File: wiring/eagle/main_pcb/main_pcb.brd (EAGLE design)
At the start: 100.1 x 79.8 mm, 19 parts

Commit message: Increase insulation around spacer holes to 5mm
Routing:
- net UC_TRIG: track 57.3 -> 55.6 mm
- net UC_ECHO: track 37.6 -> 36.3 mm
- net +5V: track 207.3 -> 206.0 mm
- net LED_G: track 60.9 -> 60.1 mm
- net LED_R: track 54.2 -> 53.6 mm
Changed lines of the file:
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@@
 <?xml version="1.0" encoding="utf-8"?>
 <!DOCTYPE eagle SYSTEM "eagle.dtd">
-<eagle version="9.3.0">
+<eagle version="9.3.1">
 <drawing>
 <settings>
@@
 <contactref element="PIHD" pad="2"/>
 <contactref element="POWER" pad="1"/>
-<wire x1="64.262" y1="75.946" x2="64.260965625" y2="76" width="1.5" layer="16"/>
-<wire x1="53.81" y1="76" x2="64.260965625" y2="76" width="1.5" layer="16"/>
-<wire x1="64.262" y1="75.946" x2="89.662" y2="75.946" width="1.5" layer="16"/>
+<wire x1="61.976" y1="75.946" x2="61.974965625" y2="76" width="1.5" layer="16"/>
+<wire x1="53.81" y1="76" x2="61.974965625" y2="76" width="1.5" layer="16"/>
+<wire x1="61.976" y1="75.946" x2="89.662" y2="75.946" width="1.5" layer="16"/>
 <wire x1="96.774" y1="62.3379125" x2="95.29955625" y2="60.095" width="1.5" layer="16"/>
-<via x="64.008" y="62.484" extent="1-16" drill="0.8" diameter="2"/>
-<wire x1="64.262" y1="75.946" x2="64.008" y2="75.692" width="1.5" layer="1"/>
-<wire x1="64.008" y1="75.692" x2="64.008" y2="62.484" width="1.5" layer="1"/>
-<via x="64.262" y="75.946" extent="1-16" drill="0.8" diameter="2"/>
-<wire x1="58.166" y1="62.484" x2="64.008" y2="62.484" width="1.5" layer="16"/>
+<via x="61.976" y="62.484" extent="1-16" drill="0.8" diameter="2"/>
+<wire x1="61.976" y1="75.946" x2="61.976" y2="62.484" width="1.5" layer="1"/>
+<via x="61.976" y="75.946" extent="1-16" drill="0.8" diameter="2"/>
+<wire x1="58.166" y1="62.484" x2="61.976" y2="62.484" width="1.5" layer="16"/>
 <wire x1="37.592" y1="30.988" x2="37.592" y2="40.132" width="1.5" layer="16"/>
 <wire x1="37.592" y1="40.132" x2="37.592" y2="47.244" width="1.5" layer="16"/>
@@
 <wire x1="18.181175" y1="59.69" x2="18.35840625" y2="59.51276875" width="1.5" layer="16"/>
 <wire x1="18.35840625" y1="59.51276875" x2="21.23876875" y2="59.51276875" width="1.5" layer="16"/>
-<wire x1="68.07" y1="55.13" x2="68.07" y2="58.422" width="1.5" layer="16"/>
-<wire x1="68.07" y1="58.422" x2="64.008" y2="62.484" width="1.5" layer="16"/>
+<wire x1="68.07" y1="55.13" x2="68.07" y2="56.39" width="1.5" layer="16"/>
+<wire x1="68.07" y1="56.39" x2="61.976" y2="62.484" width="1.5" layer="16"/>
 <wire x1="33.5075375" y1="47.244" x2="37.592" y2="47.244" width="1.5" layer="16"/>
 <wire x1="21.23876875" y1="59.51276875" x2="33.5075375" y2="47.244" width="1.5" layer="16"/>
@@
 <contactref element="R3" pad="1"/>
 <contactref element="PIHD" pad="12"/>
-<wire x1="70.612" y1="42.67575625" x2="70.612" y2="60.198" width="1.5" layer="16"/>
+<wire x1="70.612" y1="42.67575625" x2="70.612" y2="57.912" width="1.5" layer="16"/>
 <wire x1="58.928" y1="69.088" x2="58.928" y2="65.532" width="1.5" layer="16"/>
-<wire x1="58.928" y1="65.532" x2="65.278" y2="65.532" width="1.5" layer="16"/>
-<wire x1="65.278" y1="65.532" x2="70.612" y2="60.198" width="1.5" layer="16"/>
+<wire x1="58.928" y1="65.532" x2="62.992" y2="65.532" width="1.5" layer="16"/>
+<wire x1="62.992" y1="65.532" x2="70.612" y2="57.912" width="1.5" layer="16"/>
 <wire x1="68.07" y1="42.43" x2="70.36624375" y2="42.43" width="1.5" layer="16"/>
 <wire x1="70.36624375" y1="42.43" x2="70.612" y2="42.67575625" width="1.5" layer="16"/>
@@
 <contactref element="G_LED" pad="A"/>
 <via x="28.956" y="20.32" extent="1-16" drill="0.8" diameter="2"/>
-<via x="21.336" y="5.588" extent="1-16" drill="0.8" diameter="2"/>
-<wire x1="21.336" y1="5.588" x2="15.24" y2="5.588" width="1.5" layer="16"/>
+<via x="20.066" y="5.588" extent="1-16" drill="0.8" diameter="2"/>
+<wire x1="20.066" y1="5.588" x2="15.24" y2="5.588" width="1.5" layer="16"/>
 <wire x1="28.956" y1="20.32" x2="47.9678375" y2="20.32" width="1.5" layer="16"/>
 <wire x1="47.9678375" y1="20.32" x2="48.6898375" y2="19.598" width="1.5" layer="16"/>
 <wire x1="48.6898375" y1="19.598" x2="65.502" y2="19.598" width="1.5" layer="16"/>
 <wire x1="65.502" y1="19.598" x2="65.53" y2="19.57" width="1.5" layer="16"/>
-<wire x1="28.956" y1="14.478" x2="28.956" y2="20.32" width="1.5" layer="1"/>
-<wire x1="21.336" y1="5.588" x2="21.336" y2="6.858" width="1.5" layer="1"/>
-<wire x1="21.336" y1="6.858" x2="28.956" y2="14.478" width="1.5" layer="1"/>
+<wire x1="28.956" y1="16.51" x2="28.956" y2="20.32" width="1.5" layer="1"/>
+<wire x1="20.066" y1="5.588" x2="20.066" y2="7.62" width="1.5" layer="1"/>
+<wire x1="20.066" y1="7.62" x2="28.956" y2="16.51" width="1.5" layer="1"/>
 </signal>
 <signal name="N$11">
@@
 <contactref element="PIHD" pad="16"/>
 <wire x1="51.27" y1="76" x2="51.308" y2="72.644" width="1.5" layer="16"/>
-<wire x1="73.152" y1="40.894" x2="73.152" y2="61.976" width="1.5" layer="16"/>
-<wire x1="51.308" y1="72.644" x2="62.484" y2="72.644" width="1.5" layer="16"/>
-<wire x1="62.484" y1="72.644" x2="73.152" y2="61.976" width="1.5" layer="16"/>
+<wire x1="73.152" y1="40.894" x2="73.152" y2="59.182" width="1.5" layer="16"/>
+<wire x1="51.308" y1="72.644" x2="59.69" y2="72.644" width="1.5" layer="16"/>
+<wire x1="59.69" y1="72.644" x2="73.152" y2="59.182" width="1.5" layer="16"/>
 <wire x1="69.592" y1="37.334" x2="69.58499375" y2="37.35" width="1.5" layer="16"/>
 <wire x1="68.07" y1="37.35" x2="69.58499375" y2="37.35" width="1.5" layer="16"/>
@@
 <contactref element="R7" pad="1"/>
 <contactref element="PIHD" pad="31"/>
-<wire x1="21.082" y1="2.794" x2="24.13" y2="2.794" width="1.5" layer="16"/>
-<via x="24.13" y="2.794" extent="1-16" drill="0.8" diameter="2"/>
-<wire x1="24.13" y1="2.794" x2="24.13" y2="6.096" width="1.5" layer="1"/>
+<wire x1="21.082" y1="2.794" x2="23.114" y2="2.794" width="1.5" layer="16"/>
+<via x="23.114" y="2.794" extent="1-16" drill="0.8" diameter="2"/>
+<wire x1="23.114" y1="2.794" x2="23.114" y2="6.858" width="1.5" layer="1"/>
 <via x="31.75" y="17.018" extent="1-16" drill="0.8" diameter="2"/>
-<wire x1="24.13" y1="6.096" x2="31.75" y2="13.716" width="1.5" layer="1"/>
-<wire x1="31.75" y1="13.716" x2="31.75" y2="17.018" width="1.5" layer="1"/>
+<wire x1="23.114" y1="6.858" x2="31.75" y2="15.494" width="1.5" layer="1"/>
+<wire x1="31.75" y1="15.494" x2="31.75" y2="17.018" width="1.5" layer="1"/>
 <wire x1="31.75" y1="17.018" x2="65.518" y2="17.018" width="1.5" layer="16"/>
 <wire x1="65.518" y1="17.018" x2="65.53" y2="17.03" width="1.5" layer="16"/>
 </signal>
 <signal name="SPACER_RPI_BR">
-<via x="76.5" y="4" extent="1-16" drill="1" diameter="3"/>
+<via x="76.5" y="4" extent="1-16" drill="1" diameter="5"/>
 </signal>
 <signal name="SPACER_PCB_L">
-<via x="12.5" y="71.5" extent="1-16" drill="1" diameter="4"/>
+<via x="12.5" y="71.5" extent="1-16" drill="1" diameter="5"/>
 </signal>
 <signal name="SPACER_PCB_R">
-<via x="87.5" y="71.5" extent="1-16" drill="1" diameter="4"/>
+<via x="87.5" y="71.5" extent="1-16" drill="1" diameter="5"/>
 </signal>
 <signal name="SPACER_RPI_FL">
-<via x="27.5" y="62" extent="1-16" drill="1" diameter="3"/>
+<via x="27.5" y="62" extent="1-16" drill="1" diameter="5"/>
 </signal>
 <signal name="SPACER_RPI_FR">
-<via x="76.5" y="62" extent="1-16" drill="1" diameter="3"/>
+<via x="76.5" y="62" extent="1-16" drill="1" diameter="5"/>
 </signal>
 <signal name="SPACER_RPI_BL">
-<via x="27.5" y="4" extent="1-16" drill="1" diameter="3"/>
+<via x="27.5" y="4" extent="1-16" drill="1" diameter="5"/>
 </signal>
 </signals>

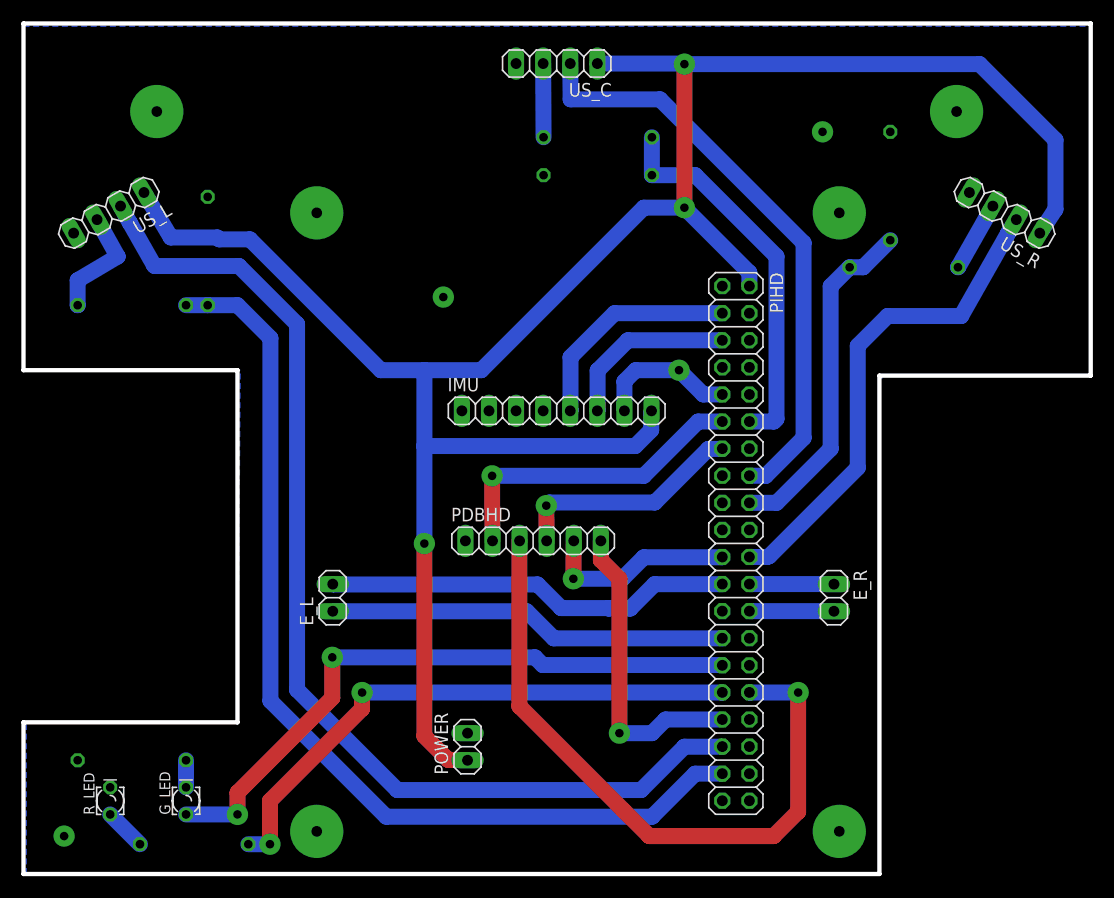
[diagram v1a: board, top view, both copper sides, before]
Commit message: Add IMU spacer and other minor adjustments
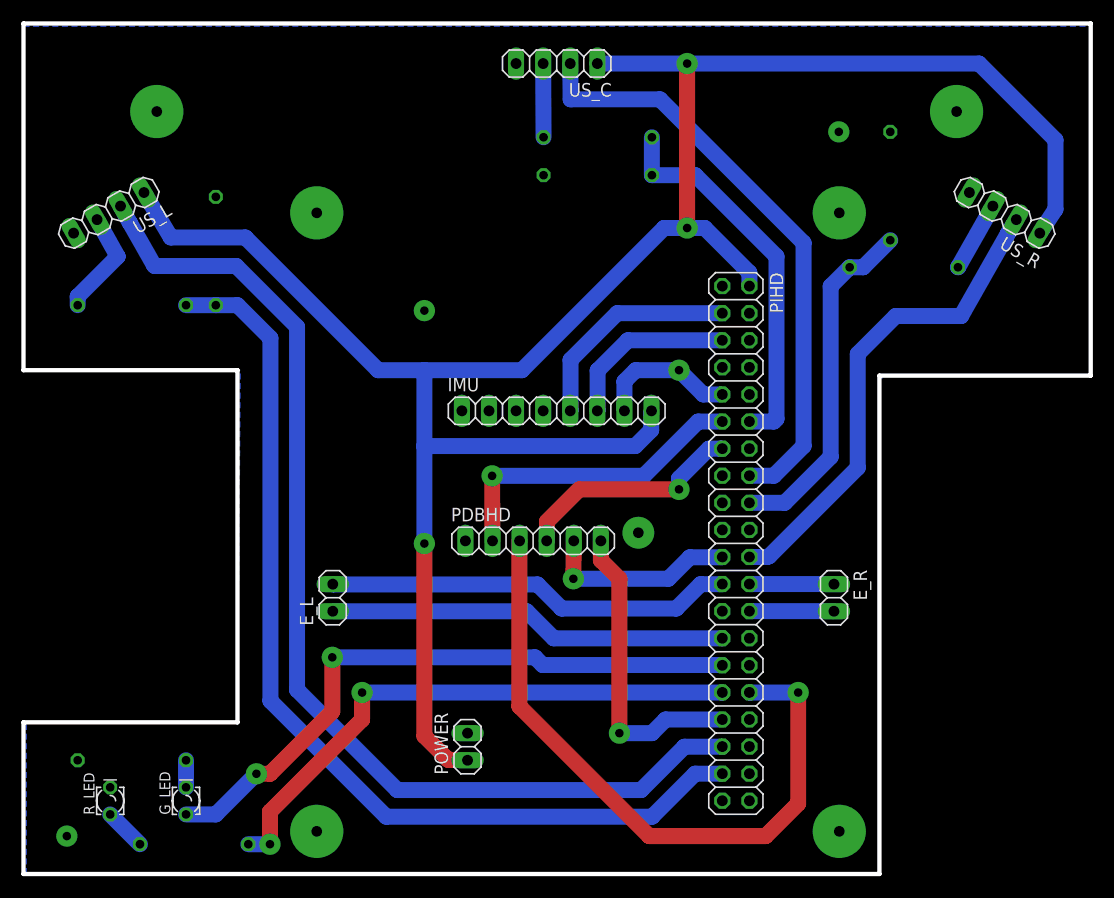
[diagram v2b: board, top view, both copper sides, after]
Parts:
- moved R2 0.76 mm to (18.0, 58.4)
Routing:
- net UL_ECHO_5V: track 10.7 -> 10.1 mm
